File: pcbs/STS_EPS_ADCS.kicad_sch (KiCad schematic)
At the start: 6 parts, among them U10 MAX11632EEGT, U5 MAX11632EEGT, U6 MAX11632EEGT, U7 MAX11632EEGT, U8 MAX11632EEGT, U9 MAX11632EEGT

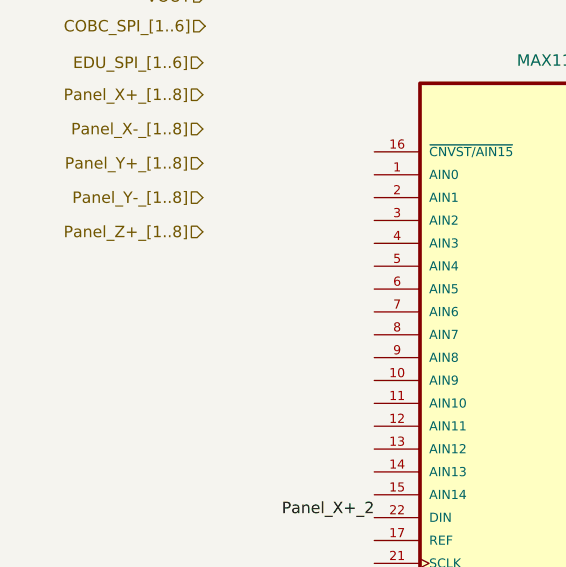
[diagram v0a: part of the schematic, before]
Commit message: Worked on STS_EPS_1.
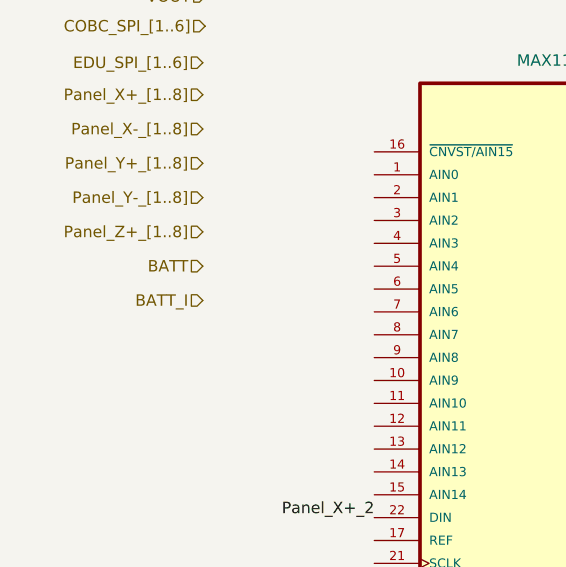
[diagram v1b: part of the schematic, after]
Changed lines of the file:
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@@
+    (effects (font (size 1.27 1.27)) (justify right))
+  )
+  (hierarchical_label "BATT" (shape input) (at 29.21 46.99 180)
     (effects (font (size 1.27 1.27)) (justify right))
   )
@@
     (effects (font (size 1.27 1.27)) (justify right))
   )
+  (hierarchical_label "BATT_I" (shape input) (at 29.21 50.8 180)
+    (effects (font (size 1.27 1.27)) (justify right))
+  )

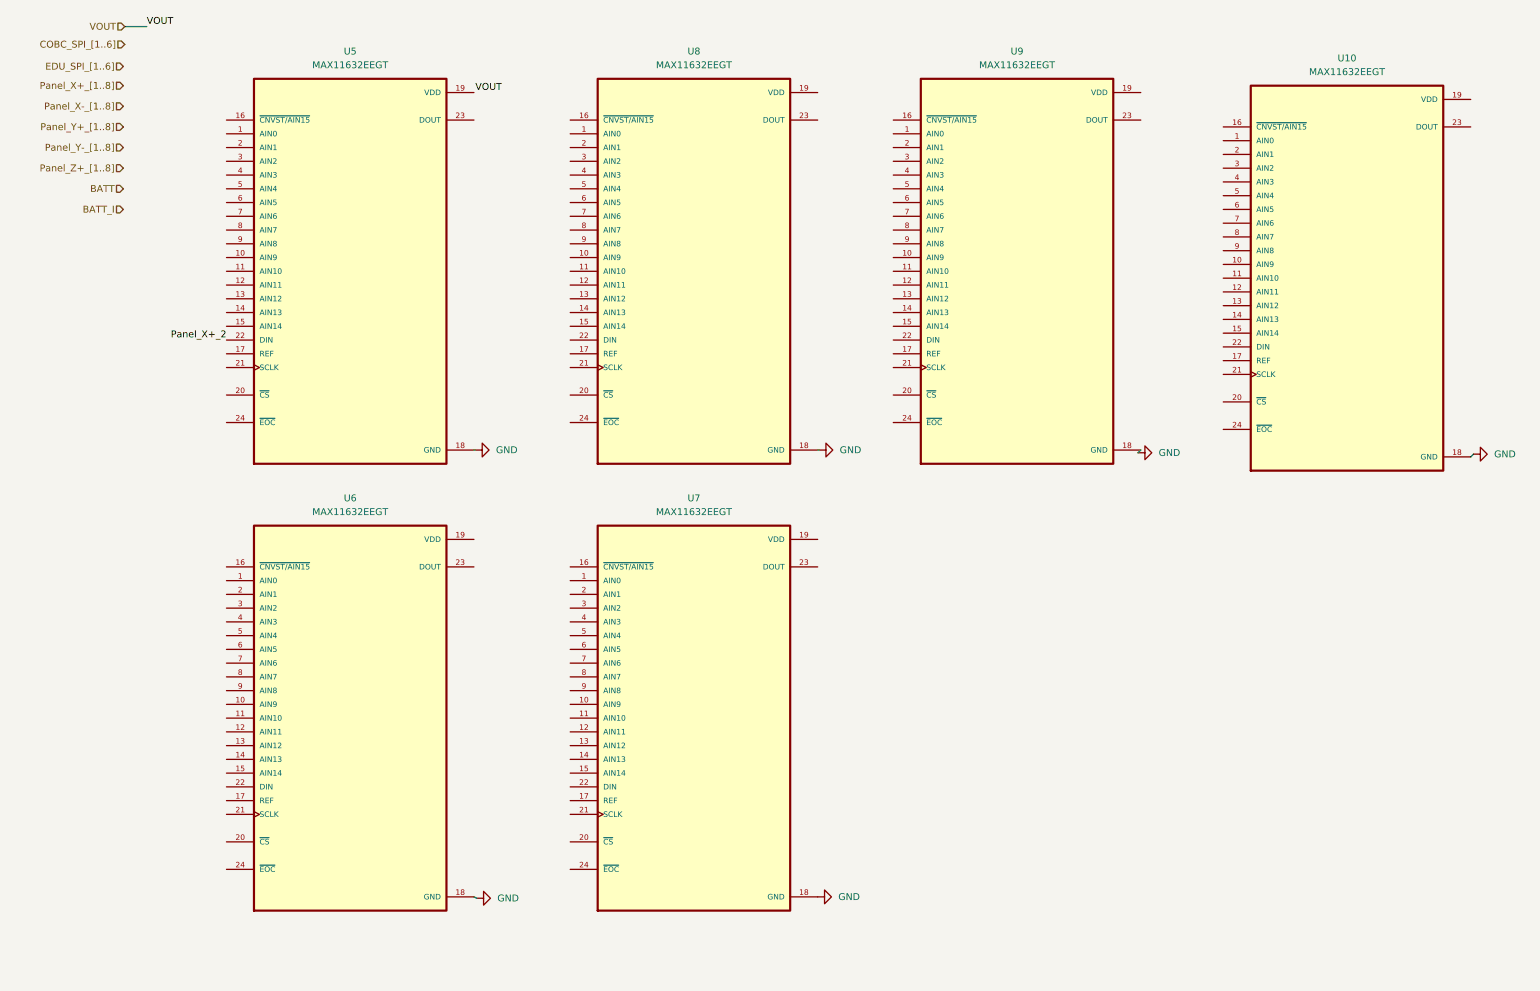
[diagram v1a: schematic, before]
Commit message: Worked on STS1_EPS_1.
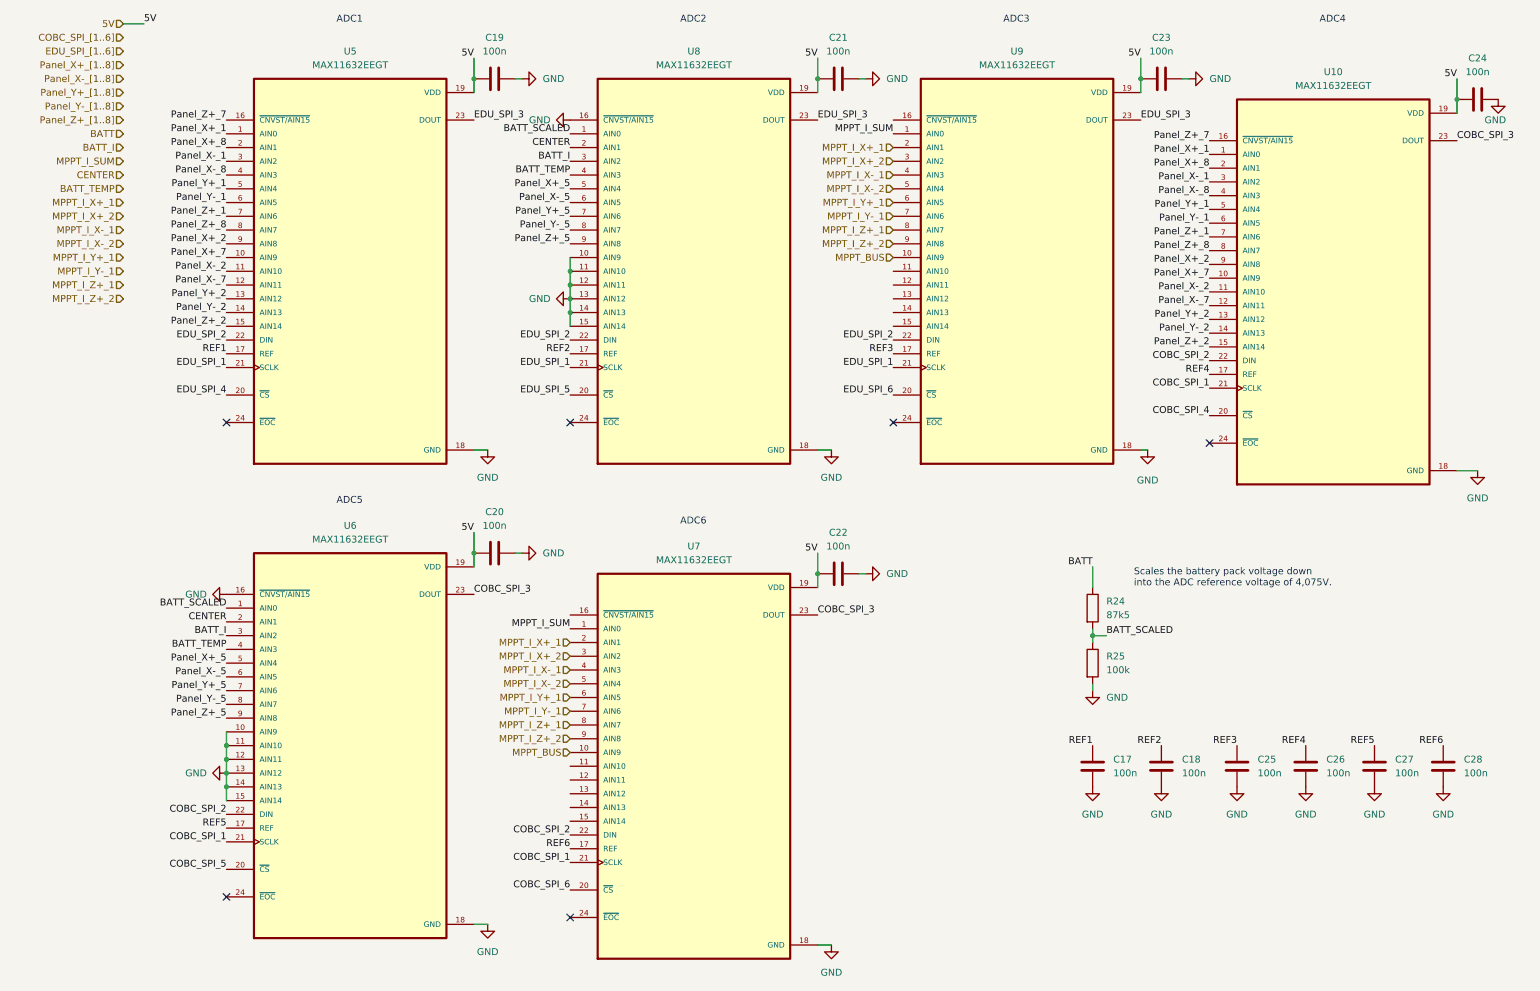
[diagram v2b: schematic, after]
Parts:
- added C17, C18, C19, C20, C21, C22, C23, C24, C25, C26, C27, C28: 100n, Capacitor_SMD:C_0805_2012Metric, symbol Device:C
- added R24: 87k5, Resistor_SMD:R_0805_2012Metric, symbol Device:R
- added R25: 100k, Resistor_SMD:R_0805_2012Metric, symbol Device:R
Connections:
- net BATT: now also R24.1
- net BATT_I: now also U6.3 (AIN2), U8.3 (AIN2)
- net GND: now also U6.10 (AIN9), U6.11 (AIN10), U6.12 (AIN11), U6.13 (AIN12), U6.14 (AIN13), U6.15 (AIN14), U6.16 (~{CNVST/AIN15}), U8.10 (AIN9), U8.11 (AIN10), U8.12 (AIN11), U8.13 (AIN12), U8.14 (AIN13), U8.15 (AIN14), U8.16 (~{CNVST/AIN15}), C17.1, C18.1, C19.2, C20.2, C21.2, C22.2, C23.2, C24.2, C25.1, C26.1, C27.1, C28.1, R25.2
- net Panel_X+_2: now also U10.9 (AIN8), U5.9 (AIN8); no longer U5.22 (DIN)
- net Panel_X+_1: now reaches U5.1 (AIN0)
- net Panel_X+_1: now also U10.1 (AIN0)
- net Panel_X+_7: now reaches U5.10 (AIN9)
- net Panel_X+_7: now also U10.10 (AIN9)
- net Panel_X-_2: now reaches U5.11 (AIN10)
- net Panel_X-_2: now also U10.11 (AIN10)
- net Panel_X-_7: now reaches U5.12 (AIN11)
- net Panel_X-_7: now also U10.12 (AIN11)
- net Panel_Y+_2: now reaches U5.13 (AIN12)
- net Panel_Y+_2: now also U10.13 (AIN12)
- net Panel_Y-_2: now reaches U5.14 (AIN13)
- net Panel_Y-_2: now also U10.14 (AIN13)
- net Panel_Z+_2: now reaches U5.15 (AIN14)
- net Panel_Z+_2: now also U10.15 (AIN14)
- net Panel_Z+_7: now reaches U5.16 (~{CNVST/AIN15})
- net Panel_Z+_7: now also U10.16 (~{CNVST/AIN15})
- net REF1: now reaches U5.17 (REF)
- net REF1: now also C17.2
- net 5V: now reaches U5.19 (VDD)
- net 5V: now also U10.19 (VDD), U6.19 (VDD), U7.19 (VDD), U8.19 (VDD), U9.19 (VDD), C19.1, C20.1, C21.1, C22.1, C23.1, C24.1
- net Panel_X+_8: now reaches U5.2 (AIN1)
- net Panel_X+_8: now also U10.2 (AIN1)
- net EDU_SPI_4: now reaches U5.20 (~{CS})
- net EDU_SPI_1: now reaches U5.21 (SCLK)
- net EDU_SPI_1: now also U8.21 (SCLK), U9.21 (SCLK)
- net EDU_SPI_3: now reaches U5.23 (DOUT)
- net EDU_SPI_3: now also U8.23 (DOUT), U9.23 (DOUT)
- net Panel_X-_1: now reaches U5.3 (AIN2)
- net Panel_X-_1: now also U10.3 (AIN2)
- net Panel_X-_8: now reaches U5.4 (AIN3)
- net Panel_X-_8: now also U10.4 (AIN3)
- net Panel_Y+_1: now reaches U5.5 (AIN4)
- net Panel_Y+_1: now also U10.5 (AIN4)
- net Panel_Y-_1: now reaches U5.6 (AIN5)
- net Panel_Y-_1: now also U10.6 (AIN5)
- net Panel_Z+_1: now reaches U5.7 (AIN6)
- net Panel_Z+_1: now also U10.7 (AIN6)
- net Panel_Z+_8: now reaches U5.8 (AIN7)
- net Panel_Z+_8: now also U10.8 (AIN7)
- net MPPT_I_SUM: now reaches U9.1 (AIN0)
- net MPPT_I_SUM: now also U7.1 (AIN0)
- net MPPT_BUS: now reaches U9.10 (AIN9)
- net MPPT_BUS: now also U7.10 (AIN9)
- net REF3: now reaches U9.17 (REF)
- net REF3: now also C25.2
- net MPPT_I_X+_1: now reaches U9.2 (AIN1)
- net MPPT_I_X+_1: now also U7.2 (AIN1)
- net EDU_SPI_6: now reaches U9.20 (~{CS})
- net EDU_SPI_2: now reaches U9.22 (DIN)
- net EDU_SPI_2: now also U5.22 (DIN), U8.22 (DIN)
- net MPPT_I_X+_2: now reaches U9.3 (AIN2)
- net MPPT_I_X+_2: now also U7.3 (AIN2)
- net MPPT_I_X-_1: now reaches U9.4 (AIN3)
- net MPPT_I_X-_1: now also U7.4 (AIN3)
- net MPPT_I_X-_2: now reaches U9.5 (AIN4)
- net MPPT_I_X-_2: now also U7.5 (AIN4)
- net MPPT_I_Y+_1: now reaches U9.6 (AIN5)
- net MPPT_I_Y+_1: now also U7.6 (AIN5)
- net MPPT_I_Y-_1: now reaches U9.7 (AIN6)
- net MPPT_I_Y-_1: now also U7.7 (AIN6)
- net MPPT_I_Z+_1: now reaches U9.8 (AIN7)
- net MPPT_I_Z+_1: now also U7.8 (AIN7)
- net MPPT_I_Z+_2: now reaches U9.9 (AIN8)
- net MPPT_I_Z+_2: now also U7.9 (AIN8)
- net BATT_SCALED: now reaches U8.1 (AIN0)
- net BATT_SCALED: now also U6.1 (AIN0), R24.2, R25.1
- net REF2: now reaches U8.17 (REF)
- net REF2: now also C18.2
- net CENTER: now reaches U8.2 (AIN1)
- net CENTER: now also U6.2 (AIN1)
- net EDU_SPI_5: now reaches U8.20 (~{CS})
- net BATT_TEMP: now reaches U8.4 (AIN3)
- net BATT_TEMP: now also U6.4 (AIN3)
- net Panel_X+_5: now reaches U8.5 (AIN4)
- net Panel_X+_5: now also U6.5 (AIN4)
- net Panel_X-_5: now reaches U8.6 (AIN5)
- net Panel_X-_5: now also U6.6 (AIN5)
- net Panel_Y+_5: now reaches U8.7 (AIN6)
- net Panel_Y+_5: now also U6.7 (AIN6)
- net Panel_Y-_5: now reaches U8.8 (AIN7)
- net Panel_Y-_5: now also U6.8 (AIN7)
- net Panel_Z+_5: now reaches U8.9 (AIN8)
- net Panel_Z+_5: now also U6.9 (AIN8)
- net REF6: now reaches U7.17 (REF)
- net REF6: now also C28.2
- net COBC_SPI_6: now reaches U7.20 (~{CS})
- net COBC_SPI_1: now reaches U7.21 (SCLK)
- net COBC_SPI_1: now also U10.21 (SCLK), U6.21 (SCLK)
- net COBC_SPI_2: now reaches U7.22 (DIN)
- net COBC_SPI_2: now also U10.22 (DIN), U6.22 (DIN)
- net COBC_SPI_3: now reaches U7.23 (DOUT)
- net COBC_SPI_3: now also U10.23 (DOUT), U6.23 (DOUT)
- net REF4: now reaches U10.17 (REF)
- net REF4: now also C26.2
- net COBC_SPI_4: now reaches U10.20 (~{CS})
- net REF5: now reaches U6.17 (REF)
- net REF5: now also C27.2
- net COBC_SPI_5: now reaches U6.20 (~{CS})
- no-connect marks 0 -> 6
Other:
- note added: "ADC1"
- note added: "ADC2"
- note added: "ADC3"
- note added: "ADC4"
- note added: "ADC5"
- note added: "ADC6"
- note added: "Scales the battery pack voltage down into the ADC reference voltage of 4,075V."
- moved on the sheet: U10, U6, U7

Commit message: Worked on STS_EPS_1.
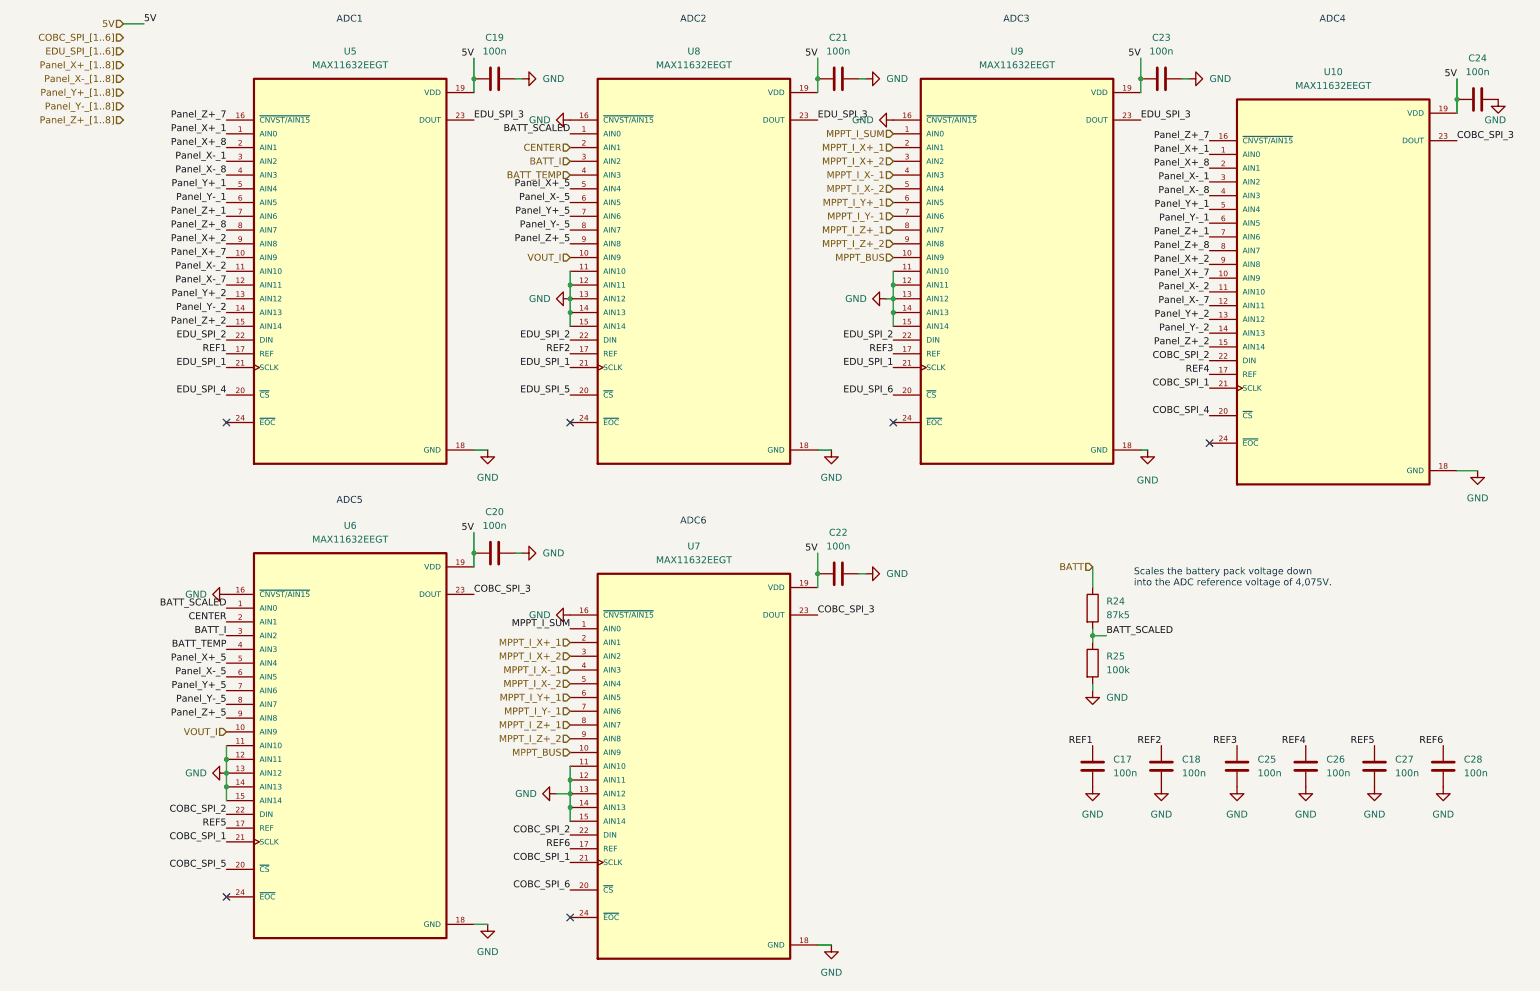
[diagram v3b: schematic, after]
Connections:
- net GND: now also U7.11 (AIN10), U7.12 (AIN11), U7.13 (AIN12), U7.14 (AIN13), U7.15 (AIN14), U7.16 (~{CNVST/AIN15}), U9.11 (AIN10), U9.12 (AIN11), U9.13 (AIN12), U9.14 (AIN13), U9.15 (AIN14), U9.16 (~{CNVST/AIN15}); no longer U6.10 (AIN9), U8.10 (AIN9)
- new net VOUT_I: U6.10 (AIN9), U8.10 (AIN9)

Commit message: Worked on STS1_EPS_1 layout.
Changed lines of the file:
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@@
-    (effects (font (size 1.27 1.27)) (justify right bottom))
-  )
-  (label "MPPT_I_SUM" (at 111.76 128.27 180)
     (effects (font (size 1.27 1.27)) (justify right bottom))
   )
@@
     (effects (font (size 1.27 1.27)) (justify right))
   )
+  (hierarchical_label "MPPT_I_SUM" (shape input) (at 111.76 128.27 180)
+    (effects (font (size 1.27 1.27)) (justify right))
+  )

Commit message: Worked on STS1_EPS_1.
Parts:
- U10, U5, U6, U7, U8, U9: footprint STS_Package_QSOP:MAX_QSOP24 -> SOP63P602X175-24N
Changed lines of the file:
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@@
     (property "Reference" "U5" (id 0) (at 71.12 21.59 0))
     (property "Value" "MAX11632EEGT" (id 1) (at 71.12 24.13 0))
-    (property "Footprint" "STS_Package_QSOP:MAX_QSOP24" (id 2) (at 71.12 62.23 0)
+    (property "Footprint" "SOP63P602X175-24N" (id 2) (at 71.12 62.23 0)
       (effects (font (size 1.27 1.27)) (justify left bottom) hide)
     )
@@
     (property "Reference" "U9" (id 0) (at 194.31 21.59 0))
     (property "Value" "MAX11632EEGT" (id 1) (at 194.31 24.13 0))
-    (property "Footprint" "STS_Package_QSOP:MAX_QSOP24" (id 2) (at 194.31 62.23 0)
+    (property "Footprint" "SOP63P602X175-24N" (id 2) (at 194.31 62.23 0)
       (effects (font (size 1.27 1.27)) (justify left bottom) hide)
     )
@@
     (property "Reference" "U8" (id 0) (at 134.62 21.59 0))
     (property "Value" "MAX11632EEGT" (id 1) (at 134.62 24.13 0))
-    (property "Footprint" "STS_Package_QSOP:MAX_QSOP24" (id 2) (at 134.62 62.23 0)
+    (property "Footprint" "SOP63P602X175-24N" (id 2) (at 134.62 62.23 0)
       (effects (font (size 1.27 1.27)) (justify left bottom) hide)
     )
@@
     (property "Reference" "U7" (id 0) (at 134.62 113.03 0))
     (property "Value" "MAX11632EEGT" (id 1) (at 134.62 115.57 0))
-    (property "Footprint" "STS_Package_QSOP:MAX_QSOP24" (id 2) (at 134.62 153.67 0)
+    (property "Footprint" "SOP63P602X175-24N" (id 2) (at 134.62 153.67 0)
       (effects (font (size 1.27 1.27)) (justify left bottom) hide)
     )
@@
     (property "Reference" "U10" (id 0) (at 252.73 25.4 0))
     (property "Value" "MAX11632EEGT" (id 1) (at 252.73 27.94 0))
-    (property "Footprint" "STS_Package_QSOP:MAX_QSOP24" (id 2) (at 252.73 66.04 0)
+    (property "Footprint" "SOP63P602X175-24N" (id 2) (at 252.73 66.04 0)
       (effects (font (size 1.27 1.27)) (justify left bottom) hide)
     )
@@
     (property "Reference" "U6" (id 0) (at 71.12 109.22 0))
     (property "Value" "MAX11632EEGT" (id 1) (at 71.12 111.76 0))
-    (property "Footprint" "STS_Package_QSOP:MAX_QSOP24" (id 2) (at 71.12 149.86 0)
-      (effects (font (size 1.27 1.27)) (justify left bottom) hide)
-    )
+    (property "Footprint" "SOP63P602X175-24N" (id 2) (at 71.12 149.86 0)
+      (effects (font (size 1.27 1.27)) (justify left bottom) hide)
+    )

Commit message: Worked on STS1_EPS_1.
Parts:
- U10, U5, U6, U7, U8, U9: footprint SOP63P602X175-24N -> STS_Package_QSOP:MAX_QSOP24
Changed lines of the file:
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@@
     (property "Reference" "U5" (id 0) (at 71.12 21.59 0))
     (property "Value" "MAX11632EEGT" (id 1) (at 71.12 24.13 0))
-    (property "Footprint" "SOP63P602X175-24N" (id 2) (at 71.12 62.23 0)
+    (property "Footprint" "STS_Package_QSOP:MAX_QSOP24" (id 2) (at 71.12 62.23 0)
       (effects (font (size 1.27 1.27)) (justify left bottom) hide)
     )
@@
     (property "Reference" "U9" (id 0) (at 194.31 21.59 0))
     (property "Value" "MAX11632EEGT" (id 1) (at 194.31 24.13 0))
-    (property "Footprint" "SOP63P602X175-24N" (id 2) (at 194.31 62.23 0)
+    (property "Footprint" "STS_Package_QSOP:MAX_QSOP24" (id 2) (at 194.31 62.23 0)
       (effects (font (size 1.27 1.27)) (justify left bottom) hide)
     )
@@
     (property "Reference" "U8" (id 0) (at 134.62 21.59 0))
     (property "Value" "MAX11632EEGT" (id 1) (at 134.62 24.13 0))
-    (property "Footprint" "SOP63P602X175-24N" (id 2) (at 134.62 62.23 0)
+    (property "Footprint" "STS_Package_QSOP:MAX_QSOP24" (id 2) (at 134.62 62.23 0)
       (effects (font (size 1.27 1.27)) (justify left bottom) hide)
     )
@@
     (property "Reference" "U7" (id 0) (at 134.62 113.03 0))
     (property "Value" "MAX11632EEGT" (id 1) (at 134.62 115.57 0))
-    (property "Footprint" "SOP63P602X175-24N" (id 2) (at 134.62 153.67 0)
+    (property "Footprint" "STS_Package_QSOP:MAX_QSOP24" (id 2) (at 134.62 153.67 0)
       (effects (font (size 1.27 1.27)) (justify left bottom) hide)
     )
@@
     (property "Reference" "U10" (id 0) (at 252.73 25.4 0))
     (property "Value" "MAX11632EEGT" (id 1) (at 252.73 27.94 0))
-    (property "Footprint" "SOP63P602X175-24N" (id 2) (at 252.73 66.04 0)
+    (property "Footprint" "STS_Package_QSOP:MAX_QSOP24" (id 2) (at 252.73 66.04 0)
       (effects (font (size 1.27 1.27)) (justify left bottom) hide)
     )
@@
     (property "Reference" "U6" (id 0) (at 71.12 109.22 0))
     (property "Value" "MAX11632EEGT" (id 1) (at 71.12 111.76 0))
-    (property "Footprint" "SOP63P602X175-24N" (id 2) (at 71.12 149.86 0)
-      (effects (font (size 1.27 1.27)) (justify left bottom) hide)
-    )
+    (property "Footprint" "STS_Package_QSOP:MAX_QSOP24" (id 2) (at 71.12 149.86 0)
+      (effects (font (size 1.27 1.27)) (justify left bottom) hide)
+    )
